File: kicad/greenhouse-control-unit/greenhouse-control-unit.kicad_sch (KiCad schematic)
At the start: 57 parts, among them J1 Screw_Terminal_01x02, J10 Conn_01x15_Female, J10_LittleBuck1 Conn_01x01_Female, J11 Conn_01x02_Male, J11_LittleBuck1 Conn_01x01_Female, J12 Screw_Terminal_01x16, J12_BigBuck1 Conn_01x01_Female, J13 Conn_01x10_Female, J13_BigBuck1 Conn_01x01_Female, J14 Conn_01x03_Male, J14_LittleBuck1 Conn_01x01_Female, J15_LittleBuck1 Conn_01x01_Female, J2 Screw_Terminal_01x02, J3 Screw_Terminal_01x02, J4 Screw_Terminal_01x02, J5 Conn_01x02_Male, J6 Conn_01x03_Male, J6_BigBuck1 Conn_01x01_Female, J7 Conn_01x10_Female, J7_BigBuck1 Conn_01x01_Female, J8 Conn_01x10_Female, J9 Conn_01x15_Female, Q1 IRLB8721PBF, Q2 2N2222A, Q3 2N2222A, Q4 2N2222A, Q5 IRLB8721PBF, Q6 IRLB8721PBF, Q7 IRLB8721PBF, Q8 IRLB8721PBF, U1 74HC595, U2 74HC595

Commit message: Replaced BJTs with FETs, used horizontal FETs
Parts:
- removed J4: Screw_Terminal_01x02, TerminalBlock_Phoenix:TerminalBlock_Phoenix_MKDS-1,5-2-5.08_1x02_P5.08mm_Horizontal, symbol Connector:Screw_Terminal_01x02
- removed Q1: IRLB8721PBF, Package_TO_SOT_THT:TO-220-3_Vertical, symbol Transistor_FET:IRLB8721PBF
- removed Q2, Q3, Q4: 2N2222A, Package_TO_SOT_THT:TO-92_Inline, symbol Nick:2N2222A
- removed R8: 2k, Resistor_THT:R_Axial_DIN0207_L6.3mm_D2.5mm_P7.62mm_Horizontal, symbol Device:R
- removed R9: 10k, Resistor_THT:R_Axial_DIN0207_L6.3mm_D2.5mm_P7.62mm_Horizontal, symbol Device:R
- added D3: LED, LED_THT:LED_D5.0mm, symbol Device:LED
- added J4: Molex_KK-254_01x02, Connector_Molex:Molex_KK-254_AE-6410-02A_1x02_P2.54mm_Vertical, symbol Connector:Conn_01x02_Male
- added Q1, Q2, Q3, Q8, Q9: 2N7000, Package_TO_SOT_THT:TO-92_Inline, symbol Transistor_FET:2N7000
- added Q4, Q5, Q6, Q7: IRLB8721PBF, Package_TO_SOT_THT:TO-220-3_Horizontal_TabDown, symbol Transistor_FET:IRLB8721PBF
- added R11: 1k, Resistor_THT:R_Axial_DIN0207_L6.3mm_D2.5mm_P7.62mm_Horizontal, symbol Device:R
- added R15, R16, R17, R18: 10k, Resistor_THT:R_Axial_DIN0207_L6.3mm_D2.5mm_P7.62mm_Horizontal, symbol Device:R
- added R6, R7: 2k, Resistor_THT:R_Axial_DIN0207_L6.3mm_D2.5mm_P7.62mm_Horizontal, symbol Device:R
- D1: footprint Package_TO_SOT_THT:TO-126-2_Vertical -> Package_TO_SOT_THT:TO-220-2_Horizontal_TabDown
- J1, J2, J3: value Screw_Terminal_01x02 -> Pluggable_Terminal_01x02
- J11: renamed from J14; value Conn_01x03_Male -> Molex_KK-254_01x03
- J12: value Screw_Terminal_01x16 -> Molex_KK-396_01x16; symbol Connector:Screw_Terminal_01x16 -> Connector:Conn_01x16_Male
- J13: value Conn_01x10_Female -> Molex_KK-254_01x10
- J14: renamed from J5; value Conn_01x02_Male -> Molex_KK-254_01x02
- J5: renamed from J6; value Conn_01x03_Male -> Molex_KK-254_01x03
- J6: renamed from J11; value Conn_01x02_Male -> Molex_KK-254_01x02
- Q10: renamed from Q6; footprint Package_TO_SOT_THT:TO-220-3_Vertical -> Package_TO_SOT_THT:TO-220-3_Horizontal_TabDown
- Q11: renamed from Q7; footprint Package_TO_SOT_THT:TO-220-3_Vertical -> Package_TO_SOT_THT:TO-220-3_Horizontal_TabDown
- Q12: renamed from Q8; footprint Package_TO_SOT_THT:TO-220-3_Vertical -> Package_TO_SOT_THT:TO-220-3_Horizontal_TabDown
- Q13: renamed from Q5; footprint Package_TO_SOT_THT:TO-220-3_Vertical -> Package_TO_SOT_THT:TO-220-3_Horizontal_TabDown
- R13: renamed from R11; value 2k -> 1k
- R14: renamed from R12; value 2k -> 1k
- R9: renamed from R10; value 4k6 -> 2k
- renumbered D3 to D6, D6 to D7, D7 to D8, R17 to R10, R7 to R12, R14 to R19, R15 to R20, R16 to R21, R13 to R22, R6 to R8
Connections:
- net PsuRelayNC_GND is gone; now on net GND: J5.2 (Pin_2)
- net PsuRelayNC_SR_Q3 is gone; now on net PsuRelayNC_Coil: U1.3 (QD)
- net +12V: now also J12.11 (Pin_11), J12.13 (Pin_13), J12.15 (Pin_15), J12.9 (Pin_9), J4.2 (Pin_2)
- net +3V3: no longer J11.1 (Pin_1)
- net +5V: now also BZ1.1 (-), D5.2 (A), J11.1 (Pin_1), J6.1 (Pin_1), Q8.3 (D), Q9.3 (D), R6.1, R7.1
- net BattRelayNC_Coil: now also D3.1 (K), J4.1 (Pin_1), Q1.3 (D)
- net BattRelayNC_SR_Q0: now also Q1.2 (G)
- net CaseFan_SR_Q2: now also Q2.2 (G)
- net GND: now also Q1.1 (S), Q2.1 (S), Q3.1 (S), Q4.3 (S), Q5.3 (S), Q6.3 (S), Q7.3 (S), R15.2, R16.2, R17.2, R18.2; no longer BZ1.2 (+), D4.1 (K), J6.2 (Pin_2), R9.2
- net Motor_IN1: now also Q9.1 (S); no longer U1.6 (QG)
- net Motor_IN2: now also Q8.1 (S); no longer U1.7 (QH)
- net SW_FET1: now also J12.4 (Pin_4), Q5.2 (D); no longer J12.2 (Pin_2), Q10.2 (D)
- net SW_FET2: now also J12.6 (Pin_6), Q6.2 (D); no longer J12.4 (Pin_4), Q11.2 (D)
- net SW_FET3: now also J12.8 (Pin_8), Q7.2 (D); no longer J12.6 (Pin_6), Q12.2 (D)
- net SW_FET4: now also J12.10 (Pin_10), Q10.2 (D); no longer J12.8 (Pin_8), Q13.2 (D)
- net StartBeep_SR_Q1: now also Q3.2 (G)
- net SW_FET5: now reaches J12.12 (Pin_12)
- net SW_FET5: now also Q11.2 (D)
- net SW_FET6: now reaches J12.14 (Pin_14)
- net SW_FET6: now also Q12.2 (D)
- net SW_FET7: now reaches J12.16 (Pin_16)
- net SW_FET7: now also Q13.2 (D)
- net at D4.2 (A): now also R7.2
- net SR_Q12 renamed SW4_SR_Q12
- net SW4_SR_Q12: now also Q10.1 (G), R19.1
- net SR_Q13 renamed SW5_SR_Q13
- net SW5_SR_Q13: now also Q11.1 (G), R20.1
- net SR_Q14 renamed SW6_SR_Q14
- net SW6_SR_Q14: now also Q12.1 (G), R21.1
- net SR_Q15 renamed SW7_SR_Q15
- net SW7_SR_Q15: now also Q13.1 (G), R22.1
- removed net SW1_SR_Q08: Q10.1 (G), R19.1, U2.15 (QA)
- removed net SW2_SR_Q09: Q11.1 (G), R20.1, U2.1 (QB)
- removed net SW3_SR_Q10: Q12.1 (G), R21.1, U2.2 (QC)
- removed net SW4_SR_Q11: Q13.1 (G), R22.1, U2.3 (QD)
- new net: D4.1 (K), J6.2 (Pin_2), Q2.3 (D)
- new net: Q3.3 (D), R11.2, R9.2
- new net: D3.2 (A), R6.2
- new net: BZ1.2 (+), R11.1
- new net SR_Q6: Q9.2 (G), U1.6 (QG)
- new net SR_Q7: Q8.2 (G), U1.7 (QH)
- new net SW0_SR_Q08: Q4.1 (G), R15.1, U2.15 (QA)
- new net SW1_SR_Q09: Q5.1 (G), R16.1, U2.1 (QB)
- new net SW2_SR_Q10: Q6.1 (G), R17.1, U2.2 (QC)
- new net SW3_SR_Q11: Q7.1 (G), R18.1, U2.3 (QD)
- new net SW_FET0: J12.2 (Pin_2), Q4.2 (D)
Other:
- note added: "Prototype TODO: - Add extra ADC - Address resistor for ADC - Move relay LED to source - Add LED to case fan FET - Change relay LED to 2k - Replace fan and relay FETs with N27000 - Add 2N7000 FETs for actuator signals - Check all R values"
- note added: "Schematic TODO: -"
- note removed: "Prototype TODO: - Reduce sensor pin headers to single block - Add easy-disconnect terminals (x6) - Try PSU relay without BJT - Reverse MC direction (rotate 90deg) - Move motor control pins to SR (remove PCF expander) - Add extra ADC - Change relay LED to 2k - Replace fan and relay FETs with N27000"
- note removed: "Schematic TODO: Replace BJTs with 2N7000 MOSFETs Replace relay IRLB with 2N7000"
- moved on the sheet: BZ1, D5, D7, D8, J11, J5, J6, Q13, R13, R14, R22, R9

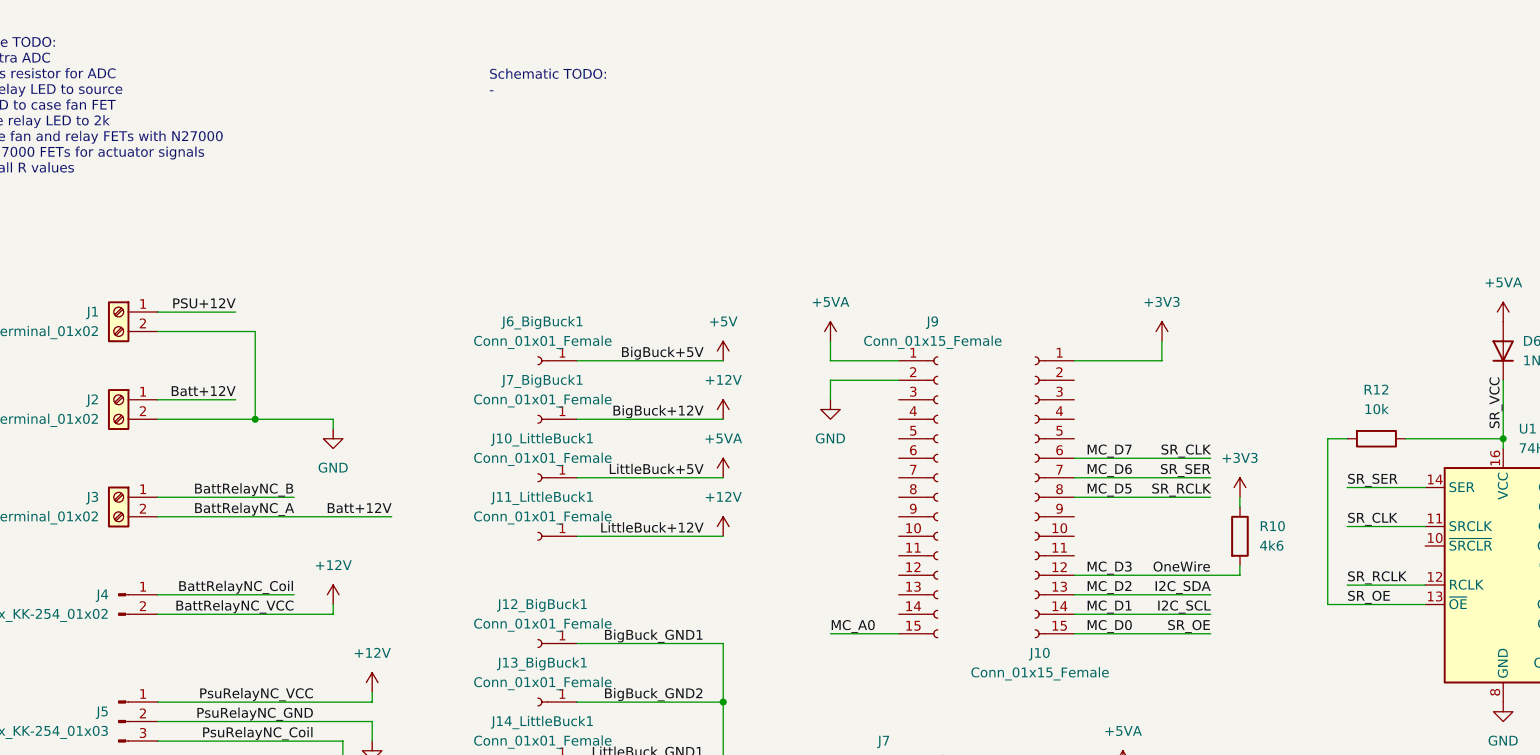
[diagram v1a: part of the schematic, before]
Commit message: Laid out PCB around new FET layout
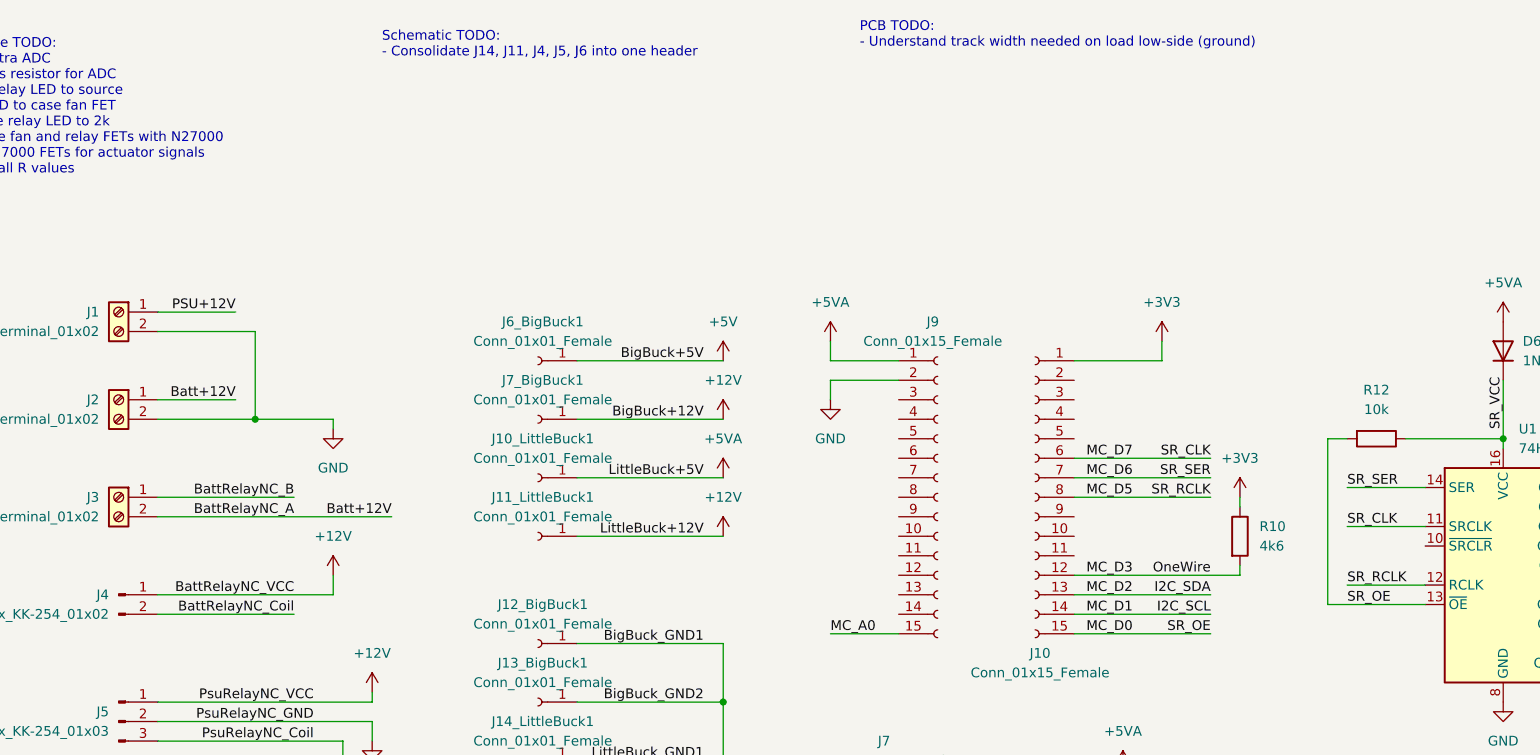
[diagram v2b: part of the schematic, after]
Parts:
- D1: footprint Package_TO_SOT_THT:TO-220-2_Horizontal_TabDown -> Package_TO_SOT_THT:TO-220-2_Vertical
- R15, R16, R17, R18, R19, R20, R21, R22: footprint Resistor_THT:R_Axial_DIN0207_L6.3mm_D2.5mm_P7.62mm_Horizontal -> Resistor_THT:R_Axial_DIN0204_L3.6mm_D1.6mm_P5.08mm_Horizontal
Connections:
- net +12V: now also J4.1 (Pin_1); no longer J4.2 (Pin_2)
- net BattRelayNC_Coil: now also J4.2 (Pin_2); no longer J4.1 (Pin_1)
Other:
- note added: "PCB TODO: - Understand track width needed on load low-side (ground)"
- note added: "Schematic TODO: - Consolidate J14, J11, J4, J5, J6 into one header"
- note removed: "Schematic TODO: -"
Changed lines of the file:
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@@
-    (stroke (width 0) (type default) (color 0 0 0 0))
-  )
-  (wire (pts (xy 81.28 95.25) (xy 81.28 93.98))
     (stroke (width 0) (type default) (color 0 0 0 0))
   )
@@
     (stroke (width 0) (type default) (color 0 0 0 0))
   )
-  (wire (pts (xy 58.42 95.25) (xy 81.28 95.25))
-    (stroke (width 0) (type default) (color 0 0 0 0))
-  )
   (wire (pts (xy 368.3 87.63) (xy 378.46 87.63))
     (stroke (width 0) (type default) (color 0 0 0 0))
@@
     (stroke (width 0) (type default) (color 0 0 0 0))
   )
+  (wire (pts (xy 58.42 95.25) (xy 76.2 95.25))
+    (stroke (width 0) (type default) (color 0 0 0 0))
+  )
   (wire (pts (xy 342.9 105.41) (xy 342.9 102.87))
     (stroke (width 0) (type default) (color 0 0 0 0))
@@
     (stroke (width 0) (type default) (color 0 0 0 0))
   )
-  (wire (pts (xy 58.42 92.71) (xy 76.2 92.71))
+  (wire (pts (xy 58.42 92.71) (xy 81.28 92.71))
     (stroke (width 0) (type default) (color 0 0 0 0))
   )
@@
     (stroke (width 0) (type default) (color 0 0 0 0))
   )
+  (wire (pts (xy 81.28 92.71) (xy 81.28 90.17))
+    (stroke (width 0) (type default) (color 0 0 0 0))
+  )
   (wire (pts (xy 157.48 156.21) (xy 180.34 156.21))
     (stroke (width 0) (type default) (color 0 0 0 0))
@@
     (effects (font (size 1.27 1.27)) (justify left bottom))
   )
+  (text "PCB TODO:\n- Understand track width needed on load low-side (ground)"
+    (at 149.86 21.59 0)
+    (effects (font (size 1.27 1.27)) (justify left bottom))
+  )
   (text "Sets address" (at 191.77 161.29 0)
     (effects (font (size 1.27 1.27)) (justify left bottom))
@@
     (effects (font (size 1.27 1.27)) (justify left bottom))
   )
-  (text "Schematic TODO:\n-" (at 101.6 27.94 0)
+  (text "Schematic TODO:\n- Consolidate J14, J11, J4, J5, J6 into one header"
+    (at 87.63 22.86 0)
     (effects (font (size 1.27 1.27)) (justify left bottom))
   )
@@
     (effects (font (size 1.27 1.27)) (justify left bottom))
   )
-  (label "BattRelayNC_Coil" (at 76.2 92.71 180)
-    (effects (font (size 1.27 1.27)) (justify right bottom))
-  )
   (label "SW_FET4" (at 368.3 97.79 0)
     (effects (font (size 1.27 1.27)) (justify left bottom))
@@
     (effects (font (size 1.27 1.27)) (justify right bottom))
   )
-  (label "BattRelayNC_VCC" (at 76.2 95.25 180)
+  (label "BattRelayNC_VCC" (at 76.2 92.71 180)
     (effects (font (size 1.27 1.27)) (justify right bottom))
   )
@@
   )
   (label "ADC2_VDD" (at 170.18 151.13 180)
+    (effects (font (size 1.27 1.27)) (justify right bottom))
+  )
+  (label "BattRelayNC_Coil" (at 76.2 95.25 180)
     (effects (font (size 1.27 1.27)) (justify right bottom))
   )
@@
       (effects (font (size 1.27 1.27)) (justify left))
     )
-    (property "Footprint" "Resistor_THT:R_Axial_DIN0207_L6.3mm_D2.5mm_P7.62mm_Horizontal" (id 2) (at 330.962 124.46 90)
+    (property "Footprint" "Resistor_THT:R_Axial_DIN0204_L3.6mm_D1.6mm_P5.08mm_Horizontal" (id 2) (at 330.962 124.46 90)
       (effects (font (size 1.27 1.27)) hide)
     )
@@
     (pin "1")
   )
-  (symbol (lib_id "power:+12V") (at 81.28 93.98 0) (unit 1)
-    (in_bom yes) (on_board yes) (fields_autoplaced)
-    (property "Reference" "#PWR02" (id 0) (at 81.28 97.79 0)
-      (effects (font (size 1.27 1.27)) hide)
-    )
-    (property "Value" "+12V" (id 1) (at 81.28 88.9 0))
-    (property "Footprint" "" (id 2) (at 81.28 93.98 0)
-      (effects (font (size 1.27 1.27)) hide)
-    )
-    (property "Datasheet" "" (id 3) (at 81.28 93.98 0)
+  (symbol (lib_id "power:+12V") (at 81.28 90.17 0) (unit 1)
+    (in_bom yes) (on_board yes) (fields_autoplaced)
+    (property "Reference" "#PWR02" (id 0) (at 81.28 93.98 0)
+      (effects (font (size 1.27 1.27)) hide)
+    )
+    (property "Value" "+12V" (id 1) (at 81.28 85.09 0))
+    (property "Footprint" "" (id 2) (at 81.28 90.17 0)
+      (effects (font (size 1.27 1.27)) hide)
+    )
+    (property "Datasheet" "" (id 3) (at 81.28 90.17 0)
       (effects (font (size 1.27 1.27)) hide)
     )
@@
       (effects (font (size 1.27 1.27)) (justify left))
     )
-    (property "Footprint" "Resistor_THT:R_Axial_DIN0207_L6.3mm_D2.5mm_P7.62mm_Horizontal" (id 2) (at 283.972 147.32 90)
+    (property "Footprint" "Resistor_THT:R_Axial_DIN0204_L3.6mm_D1.6mm_P5.08mm_Horizontal" (id 2) (at 283.972 147.32 90)
       (effects (font (size 1.27 1.27)) hide)
     )
@@
       (effects (font (size 1.27 1.27)) (justify left))
     )
-    (property "Footprint" "Resistor_THT:R_Axial_DIN0207_L6.3mm_D2.5mm_P7.62mm_Horizontal" (id 2) (at 283.972 124.46 90)
+    (property "Footprint" "Resistor_THT:R_Axial_DIN0204_L3.6mm_D1.6mm_P5.08mm_Horizontal" (id 2) (at 283.972 124.46 90)
       (effects (font (size 1.27 1.27)) hide)
     )
@@
       (effects (font (size 1.27 1.27)) (justify left))
     )
-    (property "Footprint" "Resistor_THT:R_Axial_DIN0207_L6.3mm_D2.5mm_P7.62mm_Horizontal" (id 2) (at 283.972 78.74 90)
+    (property "Footprint" "Resistor_THT:R_Axial_DIN0204_L3.6mm_D1.6mm_P5.08mm_Horizontal" (id 2) (at 283.972 78.74 90)
       (effects (font (size 1.27 1.27)) hide)
     )
@@
       (effects (font (size 1.27 1.27)) (justify left))
     )
-    (property "Footprint" "Resistor_THT:R_Axial_DIN0207_L6.3mm_D2.5mm_P7.62mm_Horizontal" (id 2) (at 330.962 78.74 90)
+    (property "Footprint" "Resistor_THT:R_Axial_DIN0204_L3.6mm_D1.6mm_P5.08mm_Horizontal" (id 2) (at 330.962 78.74 90)
       (effects (font (size 1.27 1.27)) hide)
     )
@@
       (effects (font (size 1.27 1.27)) (justify left))
     )
-    (property "Footprint" "Resistor_THT:R_Axial_DIN0207_L6.3mm_D2.5mm_P7.62mm_Horizontal" (id 2) (at 330.962 101.6 90)
+    (property "Footprint" "Resistor_THT:R_Axial_DIN0204_L3.6mm_D1.6mm_P5.08mm_Horizontal" (id 2) (at 330.962 101.6 90)
       (effects (font (size 1.27 1.27)) hide)
     )
@@
     (property "Reference" "D1" (id 0) (at 58.7375 139.7 0))
     (property "Value" "DSB20I15PA Schottky" (id 1) (at 58.7375 142.24 0))
-    (property "Footprint" "Package_TO_SOT_THT:TO-220-2_Horizontal_TabDown" (id 2) (at 58.42 146.05 0)
+    (property "Footprint" "Package_TO_SOT_THT:TO-220-2_Vertical" (id 2) (at 58.42 146.05 0)
       (effects (font (size 1.27 1.27)) hide)
     )
@@
       (effects (font (size 1.27 1.27)) (justify left))
     )
-    (property "Footprint" "Resistor_THT:R_Axial_DIN0207_L6.3mm_D2.5mm_P7.62mm_Horizontal" (id 2) (at 283.972 101.6 90)
+    (property "Footprint" "Resistor_THT:R_Axial_DIN0204_L3.6mm_D1.6mm_P5.08mm_Horizontal" (id 2) (at 283.972 101.6 90)
       (effects (font (size 1.27 1.27)) hide)
     )
@@
       (effects (font (size 1.27 1.27)) (justify left))
     )
-    (property "Footprint" "Resistor_THT:R_Axial_DIN0207_L6.3mm_D2.5mm_P7.62mm_Horizontal" (id 2) (at 330.962 147.32 90)
+    (property "Footprint" "Resistor_THT:R_Axial_DIN0204_L3.6mm_D1.6mm_P5.08mm_Horizontal" (id 2) (at 330.962 147.32 90)
       (effects (font (size 1.27 1.27)) hide)
     )
@@
     )
     (path "/84dea478-b855-4267-aa24-6b336fbce1d8"
-      (reference "D1") (unit 1) (value "DSB20I15PA Schottky") (footprint "Package_TO_SOT_THT:TO-220-2_Horizontal_TabDown")
+      (reference "D1") (unit 1) (value "DSB20I15PA Schottky") (footprint "Package_TO_SOT_THT:TO-220-2_Vertical")
     )
     (path "/856dc52a-2cad-42fc-85ba-97970f35e9b3"
@@
     )
     (path "/57cd3520-8580-4846-beb7-cc0746c295b8"
-      (reference "R15") (unit 1) (value "10k") (footprint "Resistor_THT:R_Axial_DIN0207_L6.3mm_D2.5mm_P7.62mm_Horizontal")
+      (reference "R15") (unit 1) (value "10k") (footprint "Resistor_THT:R_Axial_DIN0204_L3.6mm_D1.6mm_P5.08mm_Horizontal")
     )
     (path "/c54d3eba-4453-4389-819d-1e8a172c2e27"
-      (reference "R16") (unit 1) (value "10k") (footprint "Resistor_THT:R_Axial_DIN0207_L6.3mm_D2.5mm_P7.62mm_Horizontal")
+      (reference "R16") (unit 1) (value "10k") (footprint "Resistor_THT:R_Axial_DIN0204_L3.6mm_D1.6mm_P5.08mm_Horizontal")
     )
     (path "/442a708d-a250-40fe-a516-bbfe27973eff"
-      (reference "R17") (unit 1) (value "10k") (footprint "Resistor_THT:R_Axial_DIN0207_L6.3mm_D2.5mm_P7.62mm_Horizontal")
+      (reference "R17") (unit 1) (value "10k") (footprint "Resistor_THT:R_Axial_DIN0204_L3.6mm_D1.6mm_P5.08mm_Horizontal")
     )
     (path "/3b175832-06d9-428d-80ce-c6ee247fe233"
-      (reference "R18") (unit 1) (value "10k") (footprint "Resistor_THT:R_Axial_DIN0207_L6.3mm_D2.5mm_P7.62mm_Horizontal")
+      (reference "R18") (unit 1) (value "10k") (footprint "Resistor_THT:R_Axial_DIN0204_L3.6mm_D1.6mm_P5.08mm_Horizontal")
     )
     (path "/670352d2-b6dc-49f4-bcbd-e09685ade1fa"
-      (reference "R19") (unit 1) (value "10k") (footprint "Resistor_THT:R_Axial_DIN0207_L6.3mm_D2.5mm_P7.62mm_Horizontal")
+      (reference "R19") (unit 1) (value "10k") (footprint "Resistor_THT:R_Axial_DIN0204_L3.6mm_D1.6mm_P5.08mm_Horizontal")
     )
     (path "/6ea01011-4681-4edb-82f6-ee0596d04d05"
-      (reference "R20") (unit 1) (value "10k") (footprint "Resistor_THT:R_Axial_DIN0207_L6.3mm_D2.5mm_P7.62mm_Horizontal")
+      (reference "R20") (unit 1) (value "10k") (footprint "Resistor_THT:R_Axial_DIN0204_L3.6mm_D1.6mm_P5.08mm_Horizontal")
     )
     (path "/05c26d4a-615f-478f-999a-1633dfa478a7"
-      (reference "R21") (unit 1) (value "10k") (footprint "Resistor_THT:R_Axial_DIN0207_L6.3mm_D2.5mm_P7.62mm_Horizontal")
+      (reference "R21") (unit 1) (value "10k") (footprint "Resistor_THT:R_Axial_DIN0204_L3.6mm_D1.6mm_P5.08mm_Horizontal")
     )
     (path "/da0aa2e5-67a5-4840-930e-b50247cfb7af"
-      (reference "R22") (unit 1) (value "10k") (footprint "Resistor_THT:R_Axial_DIN0207_L6.3mm_D2.5mm_P7.62mm_Horizontal")
+      (reference "R22") (unit 1) (value "10k") (footprint "Resistor_THT:R_Axial_DIN0204_L3.6mm_D1.6mm_P5.08mm_Horizontal")
     )
     (path "/9c6824f3-5657-45c3-b20c-8450c4b95d0e"
